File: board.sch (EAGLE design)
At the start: 28 parts

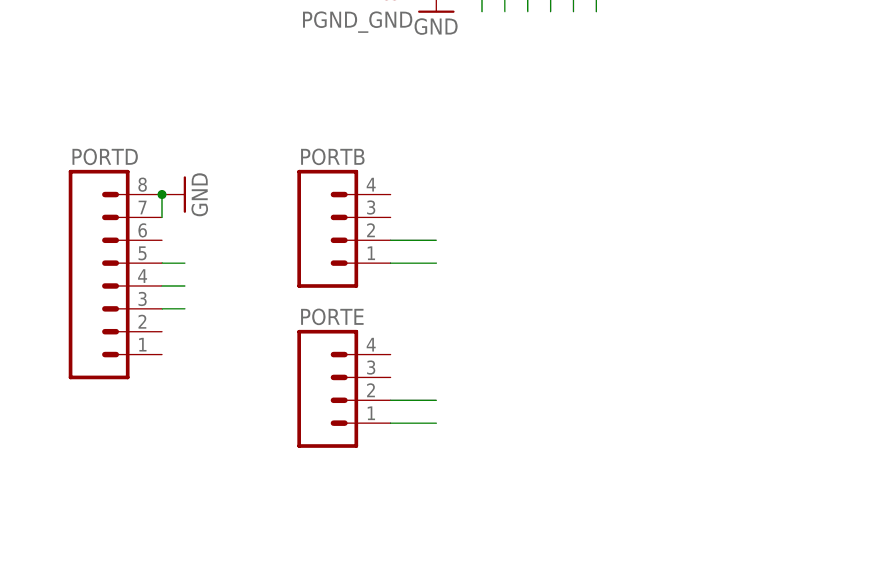
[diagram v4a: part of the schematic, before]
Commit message: connecting rest of the ports
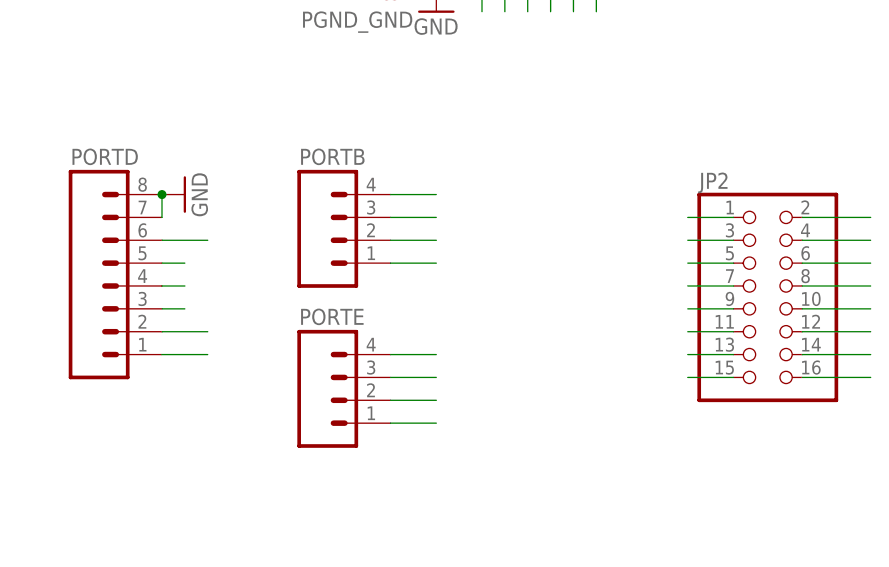
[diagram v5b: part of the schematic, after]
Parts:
- added JP2: (no value), pinhead:PINHD-2X8/90
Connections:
- removed net SCL: PORTE.2
- removed net SDA: PORTE.1
- new net PB1/VBAT_SENSE: JP2.3, PORTB.2
- new net PB2: JP2.5, PORTB.3
- new net PB3: JP2.7, PORTB.4
- new net PD0: JP2.9, PORTD.1
- new net PD1: JP2.11, PORTD.2
- new net PD5: JP2.15, PORTD.6
- new net PE1/SCL: JP2.4, PORTE.2
- new net PE1/SDA: JP2.2, PORTE.1
- new net PE2: JP2.6, PORTE.3
- new net PE3: JP2.8, PORTE.4
- net +3V3: now also JP2.12
- net GND: now also JP2.10, JP2.13
- net PB0/XMEGA_AREF: now also JP2.1
- net VBAT_SENSE: no longer PORTB.2
- net XMEGA_RX1: now also JP2.14
- net XMEGA_TX1: now also JP2.16
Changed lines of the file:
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@@
 <part name="GND9" library="supply1" deviceset="GND" device=""/>
 <part name="C3" library="rcl" deviceset="C-EU" device="C1210"/>
+<part name="JP2" library="pinhead" deviceset="PINHD-2X8" device="/90"/>
 </parts>
 <sheets>
@@
 <instance part="GND9" gate="1" x="33.02" y="86.36"/>
 <instance part="C3" gate="G$1" x="129.54" y="152.4" rot="R90"/>
+<instance part="JP2" gate="A" x="144.78" y="96.52"/>
 </instances>
 <busses>
@@
 <pinref part="GND9" gate="1" pin="GND"/>
 </segment>
+<segment>
+<pinref part="JP2" gate="A" pin="10"/>
+<wire x1="149.86" y1="93.98" x2="157.48" y2="93.98" width="0.1524" layer="91"/>
+</segment>
+<segment>
+<pinref part="JP2" gate="A" pin="13"/>
+<wire x1="142.24" y1="88.9" x2="137.16" y2="88.9" width="0.1524" layer="91"/>
+</segment>
 </net>
 <net name="VBAT" class="1">
@@
 </segment>
 </net>
-<net name="SDA" class="0">
+<net name="PE1/SDA" class="0">
 <segment>
 <pinref part="PORTE" gate="G$1" pin="1"/>
 <wire x1="104.14" y1="81.28" x2="109.22" y2="81.28" width="0.1524" layer="91"/>
 </segment>
-</net>
-<net name="SCL" class="0">
+<segment>
+<pinref part="JP2" gate="A" pin="2"/>
+<wire x1="149.86" y1="104.14" x2="157.48" y2="104.14" width="0.1524" layer="91"/>
+</segment>
+</net>
+<net name="PE1/SCL" class="0">
 <segment>
 <pinref part="PORTE" gate="G$1" pin="2"/>
 <wire x1="104.14" y1="83.82" x2="109.22" y2="83.82" width="0.1524" layer="91"/>
 </segment>
+<segment>
+<pinref part="JP2" gate="A" pin="4"/>
+<wire x1="149.86" y1="101.6" x2="157.48" y2="101.6" width="0.1524" layer="91"/>
+</segment>
 </net>
 <net name="VXMEGA_USB" class="0">
@@
 <wire x1="50.8" y1="106.68" x2="53.34" y2="106.68" width="0.1524" layer="91"/>
 </segment>
+<segment>
+<pinref part="JP2" gate="A" pin="16"/>
+<wire x1="149.86" y1="86.36" x2="157.48" y2="86.36" width="0.1524" layer="91"/>
+</segment>
 </net>
 <net name="XMEGA_RX1" class="0">
@@
 <pinref part="PORTC" gate="G$1" pin="7"/>
 <wire x1="50.8" y1="104.14" x2="53.34" y2="104.14" width="0.1524" layer="91"/>
+</segment>
+<segment>
+<pinref part="JP2" gate="A" pin="14"/>
+<wire x1="149.86" y1="88.9" x2="157.48" y2="88.9" width="0.1524" layer="91"/>
 </segment>
 </net>
@@
 <junction x="-27.94" y="106.68"/>
 <wire x1="-22.86" y1="106.68" x2="-15.24" y2="106.68" width="0.1524" layer="91"/>
-</segment>
-<segment>
-<pinref part="PORTB" gate="G$1" pin="2"/>
-<wire x1="104.14" y1="101.6" x2="109.22" y2="101.6" width="0.1524" layer="91"/>
 </segment>
 </net>
@@
 <pinref part="+3V2" gate="G$1" pin="+3V3"/>
 </segment>
+<segment>
+<pinref part="JP2" gate="A" pin="12"/>
+<wire x1="149.86" y1="91.44" x2="157.48" y2="91.44" width="0.1524" layer="91"/>
+</segment>
 </net>
 <net name="LED1" class="1">
@@
 <wire x1="88.9" y1="40.64" x2="93.98" y2="40.64" width="0.1524" layer="91"/>
 </segment>
+<segment>
+<pinref part="JP2" gate="A" pin="1"/>
+<wire x1="142.24" y1="104.14" x2="137.16" y2="104.14" width="0.1524" layer="91"/>
+</segment>
 </net>
 <net name="XBEE_RESET" class="0">
@@
 </segment>
 </net>
+<net name="PB1/VBAT_SENSE" class="0">
+<segment>
+<pinref part="PORTB" gate="G$1" pin="2"/>
+<wire x1="104.14" y1="101.6" x2="109.22" y2="101.6" width="0.1524" layer="91"/>
+</segment>
+<segment>
+<pinref part="JP2" gate="A" pin="3"/>
+<wire x1="142.24" y1="101.6" x2="137.16" y2="101.6" width="0.1524" layer="91"/>
+</segment>
+</net>
+<net name="PB2" class="0">
+<segment>
+<pinref part="PORTB" gate="G$1" pin="3"/>
+<wire x1="104.14" y1="104.14" x2="109.22" y2="104.14" width="0.1524" layer="91"/>
+</segment>
+<segment>
+<pinref part="JP2" gate="A" pin="5"/>
+<wire x1="142.24" y1="99.06" x2="137.16" y2="99.06" width="0.1524" layer="91"/>
+</segment>
+</net>
+<net name="PB3" class="0">
+<segment>
+<pinref part="PORTB" gate="G$1" pin="4"/>
+<wire x1="104.14" y1="106.68" x2="109.22" y2="106.68" width="0.1524" layer="91"/>
+</segment>
+<segment>
+<pinref part="JP2" gate="A" pin="7"/>
+<wire x1="142.24" y1="96.52" x2="137.16" y2="96.52" width="0.1524" layer="91"/>
+</segment>
+</net>
+<net name="PE2" class="0">
+<segment>
+<pinref part="PORTE" gate="G$1" pin="3"/>
+<wire x1="104.14" y1="86.36" x2="109.22" y2="86.36" width="0.1524" layer="91"/>
+</segment>
+<segment>
+<pinref part="JP2" gate="A" pin="6"/>
+<wire x1="149.86" y1="99.06" x2="157.48" y2="99.06" width="0.1524" layer="91"/>
+</segment>
+</net>
+<net name="PE3" class="0">
+<segment>
+<pinref part="PORTE" gate="G$1" pin="4"/>
+<wire x1="104.14" y1="88.9" x2="109.22" y2="88.9" width="0.1524" layer="91"/>
+</segment>
+<segment>
+<pinref part="JP2" gate="A" pin="8"/>
+<wire x1="149.86" y1="96.52" x2="157.48" y2="96.52" width="0.1524" layer="91"/>
+</segment>
+</net>
+<net name="PD0" class="0">
+<segment>
+<pinref part="PORTD" gate="G$1" pin="1"/>
+<wire x1="78.74" y1="88.9" x2="83.82" y2="88.9" width="0.1524" layer="91"/>
+</segment>
+<segment>
+<pinref part="JP2" gate="A" pin="9"/>
+<wire x1="142.24" y1="93.98" x2="137.16" y2="93.98" width="0.1524" layer="91"/>
+</segment>
+</net>
+<net name="PD1" class="0">
+<segment>
+<pinref part="PORTD" gate="G$1" pin="2"/>
+<wire x1="78.74" y1="91.44" x2="83.82" y2="91.44" width="0.1524" layer="91"/>
+</segment>
+<segment>
+<pinref part="JP2" gate="A" pin="11"/>
+<wire x1="142.24" y1="91.44" x2="137.16" y2="91.44" width="0.1524" layer="91"/>
+</segment>
+</net>
+<net name="PD5" class="0">
+<segment>
+<pinref part="PORTD" gate="G$1" pin="6"/>
+<wire x1="78.74" y1="101.6" x2="83.82" y2="101.6" width="0.1524" layer="91"/>
+</segment>
+<segment>
+<pinref part="JP2" gate="A" pin="15"/>
+<wire x1="142.24" y1="86.36" x2="137.16" y2="86.36" width="0.1524" layer="91"/>
+</segment>
+</net>

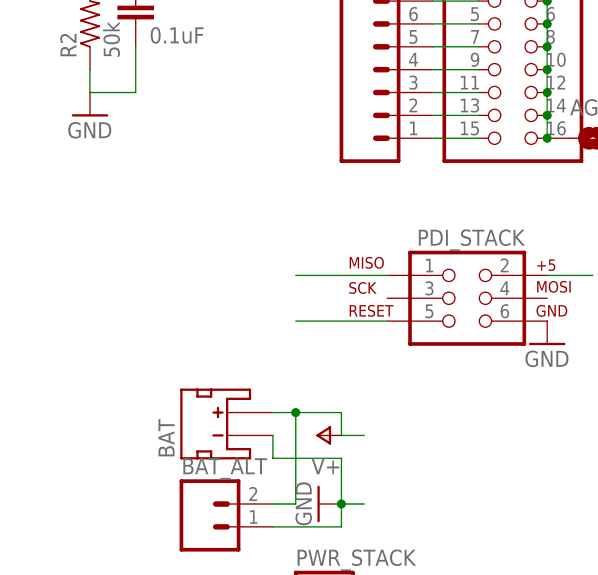
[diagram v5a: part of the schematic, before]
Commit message: adjust the AGND polygon
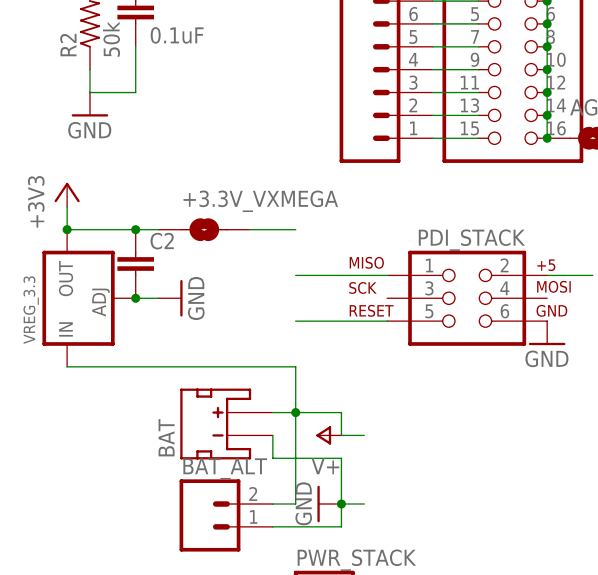
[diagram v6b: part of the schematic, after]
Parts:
- added +3.3V_VXMEGA: SOLDERJUMPERTRACE, SparkFun-Passives:SOLDERJUMPERTRACE
- added C2: (no value), rcl:C-EUC0805K
- added VREG_3.3: (no value), microbuilder:LM1117SOT223-WAVE
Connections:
- net +3V3: now also +3.3V_VXMEGA.1, C2.1, VREG_3.3.OUT
- net GND: now also C2.2, VREG_3.3.ADJ
- net VBAT: now also VREG_3.3.IN
- net VXMEGA: now also +3.3V_VXMEGA.2
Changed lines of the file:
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@@
 <part name="C3" library="rcl" deviceset="C-EU" device="C1210"/>
 <part name="JP2" library="pinhead" deviceset="PINHD-2X8" device="/90"/>
+<part name="VREG_3.3" library="microbuilder" deviceset="LM1117" device="SOT223-WAVE"/>
+<part name="GND7" library="supply1" deviceset="GND" device=""/>
+<part name="+3V3" library="supply1" deviceset="+3V3" device=""/>
+<part name="+3.3V_VXMEGA" library="SparkFun-Passives" deviceset="SOLDERJUMPER" device="TRACE"/>
+<part name="C2" library="rcl" deviceset="C-EU" device="C0805K"/>
 </parts>
 <sheets>
@@
 <instance part="C3" gate="G$1" x="129.54" y="152.4" rot="R90"/>
 <instance part="JP2" gate="A" x="144.78" y="96.52"/>
+<instance part="VREG_3.3" gate="G$1" x="-30.48" y="71.12" rot="R90"/>
+<instance part="GND7" gate="1" x="-17.78" y="71.12" rot="R90"/>
+<instance part="+3V3" gate="G$1" x="-30.48" y="83.82"/>
+<instance part="+3.3V_VXMEGA" gate="1" x="-15.24" y="78.74" smashed="yes">
+<attribute name="NAME" x="-17.78" y="81.28" size="1.778" layer="95"/>
+</instance>
+<instance part="C2" gate="G$1" x="-22.86" y="76.2"/>
 </instances>
 <busses>
@@
 <wire x1="142.24" y1="88.9" x2="137.16" y2="88.9" width="0.1524" layer="91"/>
 </segment>
+<segment>
+<pinref part="VREG_3.3" gate="G$1" pin="ADJ"/>
+<pinref part="GND7" gate="1" pin="GND"/>
+<wire x1="-20.32" y1="71.12" x2="-22.86" y2="71.12" width="0.1524" layer="91"/>
+<pinref part="C2" gate="G$1" pin="2"/>
+<junction x="-22.86" y="71.12"/>
+</segment>
 </net>
 <net name="VBAT" class="1">
@@
 <wire x1="-5.08" y1="48.26" x2="-5.08" y2="58.42" width="0.1524" layer="91"/>
 <junction x="-5.08" y="58.42"/>
+<wire x1="-5.08" y1="58.42" x2="-5.08" y2="63.5" width="0.1524" layer="91"/>
+<pinref part="VREG_3.3" gate="G$1" pin="IN"/>
+<wire x1="-5.08" y1="63.5" x2="-30.48" y2="63.5" width="0.1524" layer="91"/>
 </segment>
 <segment>
@@
 <pinref part="PWR_STACK" gate="G$1" pin="3"/>
 <wire x1="5.08" y1="38.1" x2="10.16" y2="38.1" width="0.1524" layer="91"/>
+</segment>
+<segment>
+<pinref part="+3.3V_VXMEGA" gate="1" pin="2"/>
+<wire x1="-10.16" y1="78.74" x2="-5.08" y2="78.74" width="0.1524" layer="91"/>
 </segment>
 </net>
@@
 </segment>
 </net>
-<net name="+3V3" class="0">
+<net name="+3V3" class="1">
 <segment>
 <pinref part="+3V1" gate="G$1" pin="+3V3"/>
@@
 <wire x1="149.86" y1="91.44" x2="157.48" y2="91.44" width="0.1524" layer="91"/>
 </segment>
-</net>
+<segment>
+<pinref part="+3V3" gate="G$1" pin="+3V3"/>
+<pinref part="VREG_3.3" gate="G$1" pin="OUT"/>
+<wire x1="-30.48" y1="81.28" x2="-30.48" y2="78.74" width="0.1524" layer="91"/>
+<pinref part="+3.3V_VXMEGA" gate="1" pin="1"/>
+<wire x1="-30.48" y1="78.74" x2="-22.86" y2="78.74" width="0.1524" layer="91"/>
+<junction x="-30.48" y="78.74"/>
+<pinref part="C2" gate="G$1" pin="1"/>
+<wire x1="-22.86" y1="78.74" x2="-20.32" y2="78.74" width="0.1524" layer="91"/>
+<junction x="-22.86" y="78.74"/>
+</segment>
+</net>

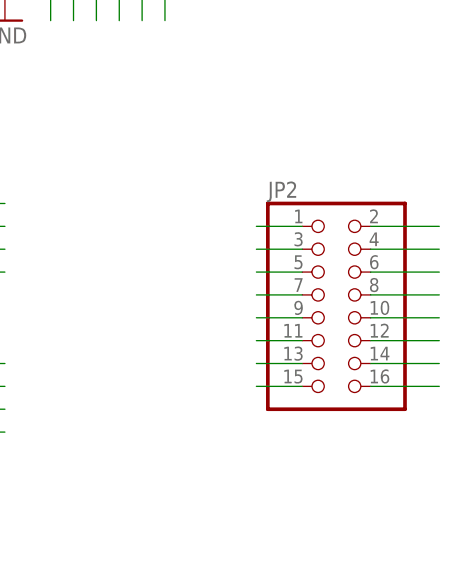
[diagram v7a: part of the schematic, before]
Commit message: on a second thought, do not put that power pin in the middle of the connector...
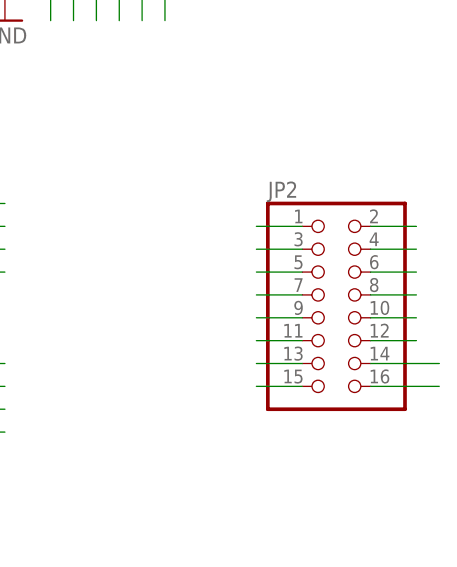
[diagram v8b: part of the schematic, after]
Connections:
- removed net PE1/SDA: JP2.2, PORTE.1
- new net PE0/SDA: JP2.6, PORTE.1
- net +3V3: now also JP2.2; no longer JP2.12
- net GND: now also JP2.4; no longer JP2.10
- net PE1/SCL: now also JP2.8; no longer JP2.4
- net PE2: now also JP2.10; no longer JP2.6
- net PE3: now also JP2.12; no longer JP2.8
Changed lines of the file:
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@@
-</segment>
-<segment>
-<pinref part="JP2" gate="A" pin="10"/>
-<wire x1="149.86" y1="93.98" x2="157.48" y2="93.98" width="0.1524" layer="91"/>
 </segment>
 <segment>
@@
 <pinref part="C2" gate="G$1" pin="2"/>
 <junction x="-22.86" y="71.12"/>
+</segment>
+<segment>
+<pinref part="JP2" gate="A" pin="4"/>
+<wire x1="149.86" y1="101.6" x2="154.94" y2="101.6" width="0.1524" layer="91"/>
 </segment>
 </net>
@@
 </segment>
 </net>
-<net name="PE1/SDA" class="0">
+<net name="PE0/SDA" class="0">
 <segment>
 <pinref part="PORTE" gate="G$1" pin="1"/>
@@
 </segment>
 <segment>
-<pinref part="JP2" gate="A" pin="2"/>
-<wire x1="149.86" y1="104.14" x2="157.48" y2="104.14" width="0.1524" layer="91"/>
+<pinref part="JP2" gate="A" pin="6"/>
+<wire x1="149.86" y1="99.06" x2="154.94" y2="99.06" width="0.1524" layer="91"/>
 </segment>
 </net>
@@
 </segment>
 <segment>
-<pinref part="JP2" gate="A" pin="4"/>
-<wire x1="149.86" y1="101.6" x2="157.48" y2="101.6" width="0.1524" layer="91"/>
+<pinref part="JP2" gate="A" pin="8"/>
+<wire x1="149.86" y1="96.52" x2="154.94" y2="96.52" width="0.1524" layer="91"/>
 </segment>
 </net>
@@
 </segment>
 <segment>
-<pinref part="JP2" gate="A" pin="12"/>
-<wire x1="149.86" y1="91.44" x2="157.48" y2="91.44" width="0.1524" layer="91"/>
-</segment>
-<segment>
 <pinref part="+3V3" gate="G$1" pin="+3V3"/>
 <pinref part="VREG_3.3" gate="G$1" pin="OUT"/>
@@
 <junction x="-22.86" y="78.74"/>
 </segment>
+<segment>
+<pinref part="JP2" gate="A" pin="2"/>
+<wire x1="149.86" y1="104.14" x2="154.94" y2="104.14" width="0.1524" layer="91"/>
+</segment>
 </net>
 <net name="LED1" class="1">
@@
 </segment>
 <segment>
-<pinref part="JP2" gate="A" pin="6"/>
-<wire x1="149.86" y1="99.06" x2="157.48" y2="99.06" width="0.1524" layer="91"/>
+<pinref part="JP2" gate="A" pin="10"/>
+<wire x1="149.86" y1="93.98" x2="154.94" y2="93.98" width="0.1524" layer="91"/>
 </segment>
 </net>
@@
 </segment>
 <segment>
-<pinref part="JP2" gate="A" pin="8"/>
-<wire x1="149.86" y1="96.52" x2="157.48" y2="96.52" width="0.1524" layer="91"/>
-</segment>
-</net>
+<pinref part="JP2" gate="A" pin="12"/>
+<wire x1="149.86" y1="91.44" x2="154.94" y2="91.44" width="0.1524" layer="91"/>
+</segment>
+</net>
